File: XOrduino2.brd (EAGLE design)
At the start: 94 x 54.1 mm, 82 parts, among them J1 2.5mm, J2 2.5mm, J3 2.5mm, J4 2.5mm, J5 Batt In, J6 MOT R, J7 MOT L, P1 10k, Q1 ALS-PT204-6C/L177, SW1 RESET, SW2 6mm Button, SW3 LEFT BUMPER, SW4 RIGHT BUMPER, U1 ATMEGA32U4-XUAU, U2 LMV358, U3 NJU7261, U4 DRV8833PWP, U5 QRE1113GR, U6 QRE1113GR, X1 USBPCB, X2 USBMINIB, X3 USBMICROB-VIA, Y1 16MHz

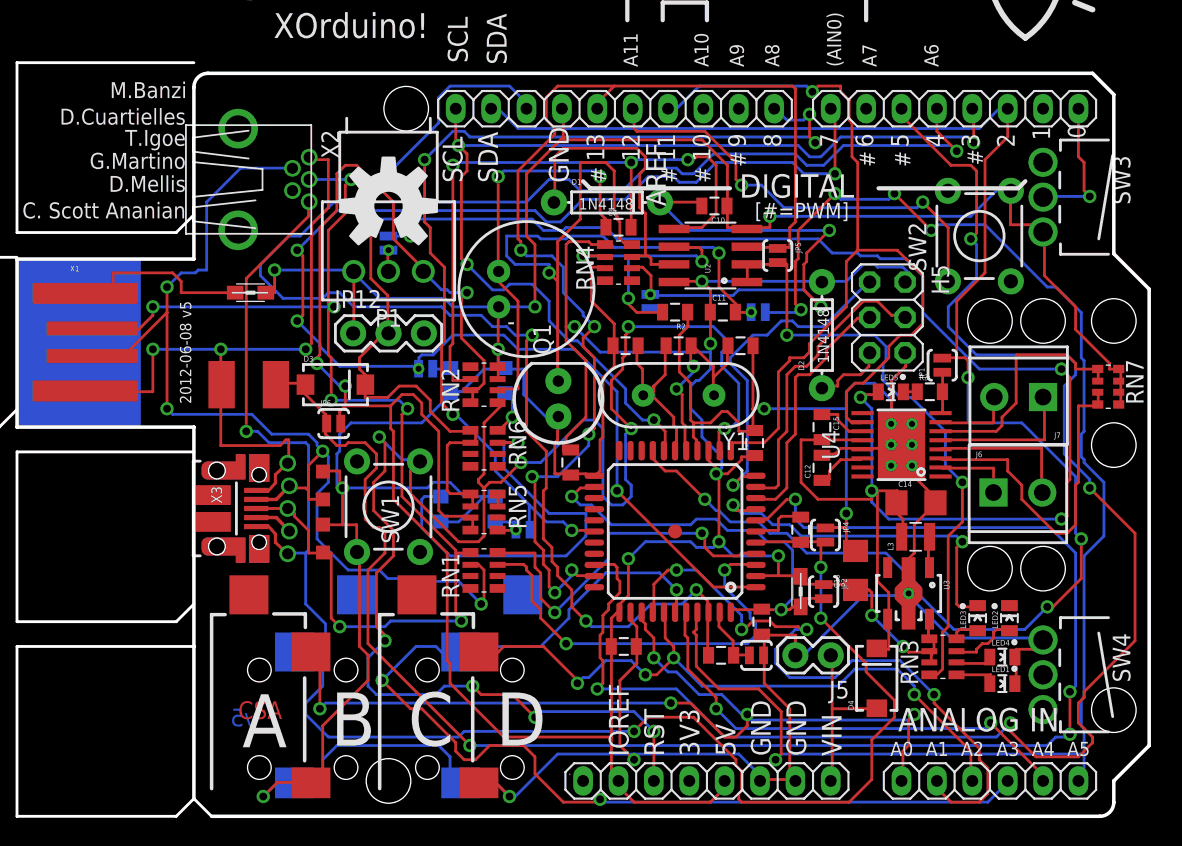
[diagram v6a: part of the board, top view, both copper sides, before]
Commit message: Best 2-layer XOrduino layout generated by Eagle.
1mil grid, diagonal route direction preference, 95% routed.
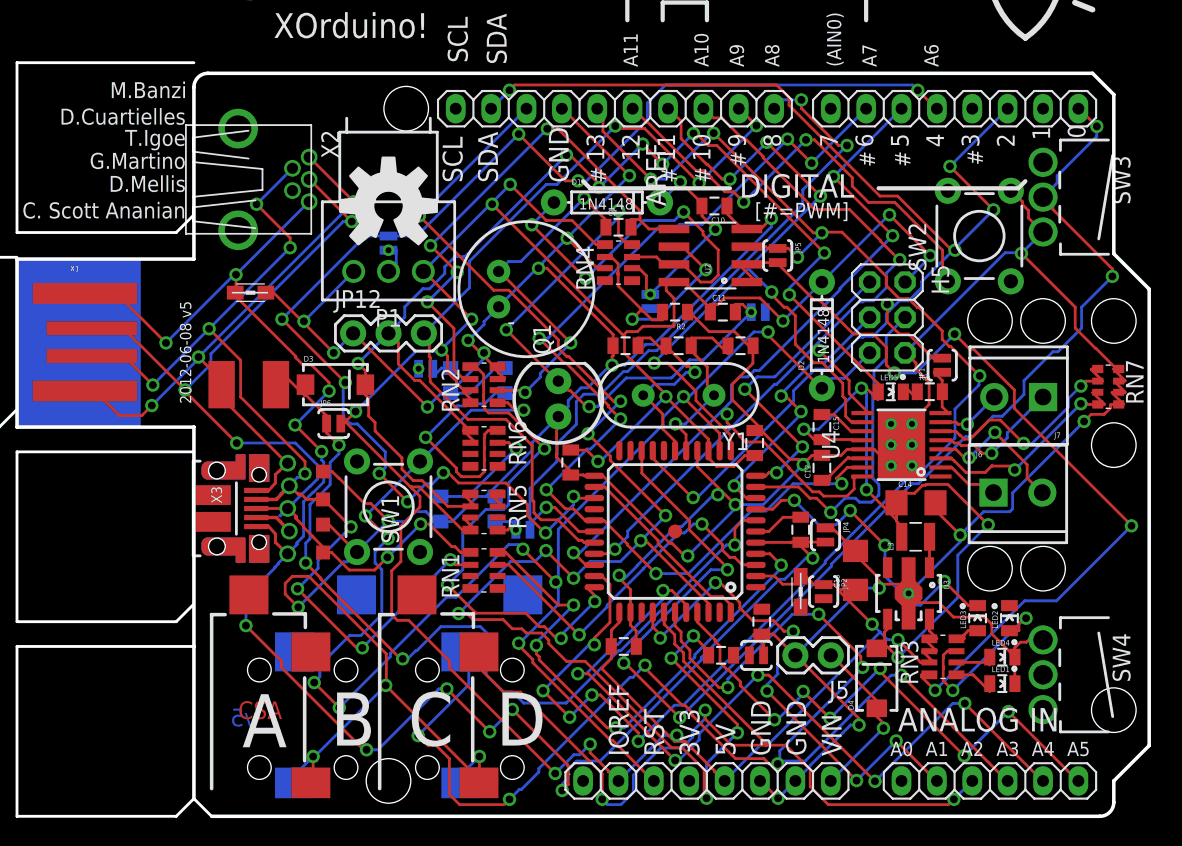
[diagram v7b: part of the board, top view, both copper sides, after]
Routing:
- net D7: track 100.4 -> 0.00 mm, vias 4 -> 0
- net D0/RX: track 10.0 -> 89.3 mm, vias 1 -> 5
- net D6*: track 0.00 -> 76.6 mm, vias 0 -> 7
- net D3/SCL: track 74.8 -> 0.00 mm, vias 4 -> 0
- net A0: track 67.5 -> 0.00 mm, vias 5 -> 0
- net A5: track 107.1 -> 41.3 mm, vias 5 -> 6
- net IO9*: track 0.00 -> 59.4 mm, vias 0 -> 3
- net IO10*: track 0.00 -> 57.0 mm, vias 0 -> 3
- net VUSB: track 119.0 -> 64.4 mm
- net D5*: track 112.6 -> 62.2 mm
- net D4: track 51.3 -> 93.8 mm, vias 3 -> 10
- net HWB: track 0.00 -> 37.9 mm, vias 0 -> 4
- net D2/SDA: track 119.1 -> 92.2 mm, vias 4 -> 6
- net AREF: track 85.8 -> 111.1 mm, vias 3 -> 12
- net A4: track 34.1 -> 58.1 mm, vias 2 -> 6
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
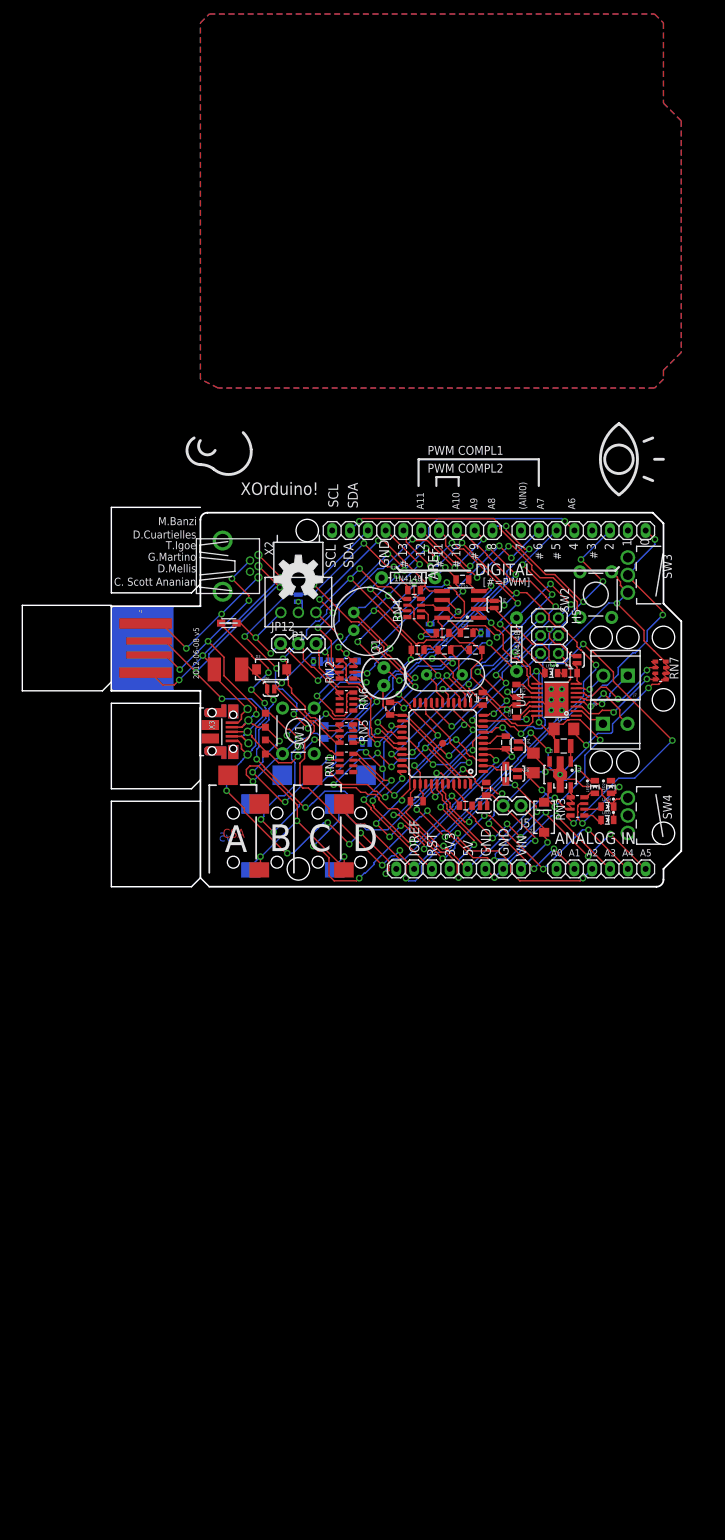
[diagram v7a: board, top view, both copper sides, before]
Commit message: Fully-routed 2-layer version of XOrduino.  Thanks to freerouting.net.
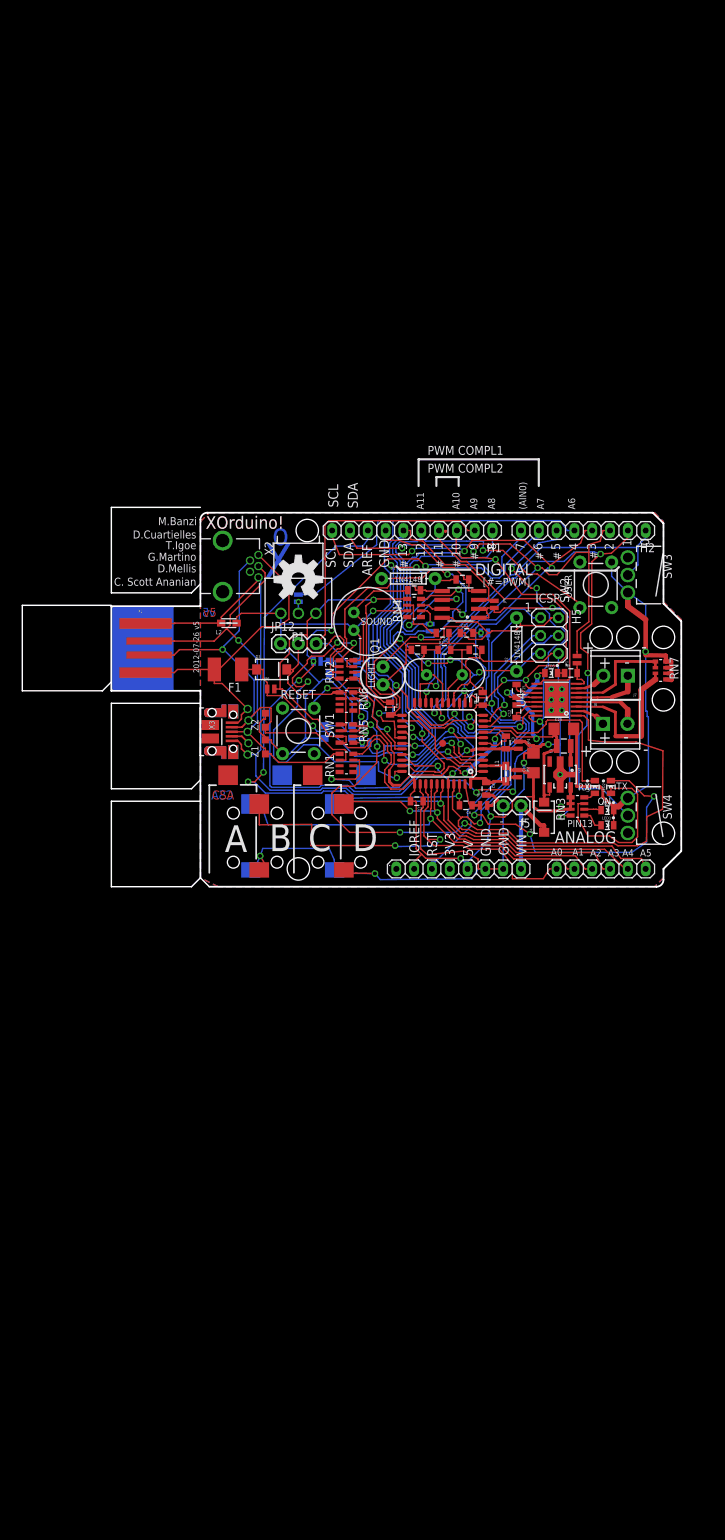
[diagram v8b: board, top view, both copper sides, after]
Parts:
- moved SW2 1.40 mm to (69.1, 43.1)
- moved LED1 0.76 mm to (70.7, 8.76)
- moved LED4 0.51 mm to (70.7, 10.9)
- moved Q1 0.18 mm to (38.7, 30.1)
- moved D1 0.13 mm to (42.4, 43.9)
- moved P1 0.13 mm to (26.7, 39.0)
- moved C6 0.05 mm to (50.5, 11.6)
- moved JP3 0.05 mm to (53.1, 11.6)
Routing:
- net D7: track 0.00 -> 100.6 mm, vias 0 -> 4
- net N$8: track 2.09 -> 99.0 mm, vias 0 -> 4
- net D1/TX: track 0.00 -> 89.2 mm, vias 0 -> 3
- net D3/SCL: track 0.00 -> 77.7 mm, vias 0 -> 4
- net TXLED: track 0.00 -> 73.1 mm, vias 0 -> 4
- net A0: track 0.00 -> 65.3 mm, vias 0 -> 2
- net A3: track 98.2 -> 49.0 mm, vias 8 -> 1
- net D0/RX: track 89.3 -> 50.2 mm, vias 5 -> 1
- net IO13*: track 104.5 -> 67.2 mm, vias 10 -> 1
- net VCCIO: track 141.1 -> 105.0 mm, vias 13 -> 5
- net IO12: track 33.1 -> 68.6 mm
- net A5: track 41.3 -> 74.5 mm, vias 6 -> 1
- net UGND: track 122.3 -> 90.7 mm, vias 12 -> 1
- net AREF: track 111.1 -> 80.0 mm, vias 12 -> 3
- net IO10*: track 57.0 -> 85.3 mm, vias 3 -> 2
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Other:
- board text added: "+"
- board text added: "-"
- board text added: "2012-07-26 v5"
- board text added: "4.5v"
- board text added: "ANALOG"
- board text added: "Battery"
- board text added: "Front Skid"
- board text added: "ICSP"
- board text added: "IN"
- board text added: "LIGHT"
- board text added: "Motors"
- board text added: "ON"
- board text added: "PIN13"
- board text added: "RESET"
- board text added: "RX"
- board text added: "SOUND"
- board text added: "Sensors"
- board text added: "Speed"
- board text added: "TX"
- board text added: "USER"
- board text added: "X"
- board text added: "o"
- board text removed: "2012-06-08 v5"
- board text removed: "ANALOG IN"
